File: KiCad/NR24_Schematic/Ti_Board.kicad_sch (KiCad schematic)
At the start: 23 parts, among them J5 J1 Pin J3 Pin, J5 J12 (CAN Interface w/ Transce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, J5 J4 Pin J2 Pin, J5 J5 Pin J7 Pin, J5 J8 Pin J6 Pin, J5 XBEE PRO, J6 SpeakON_NL2, Q1 Q_NMOS_DGS, Q2 Q_NMOS_DGS, Q3 Q_NMOS_DGS

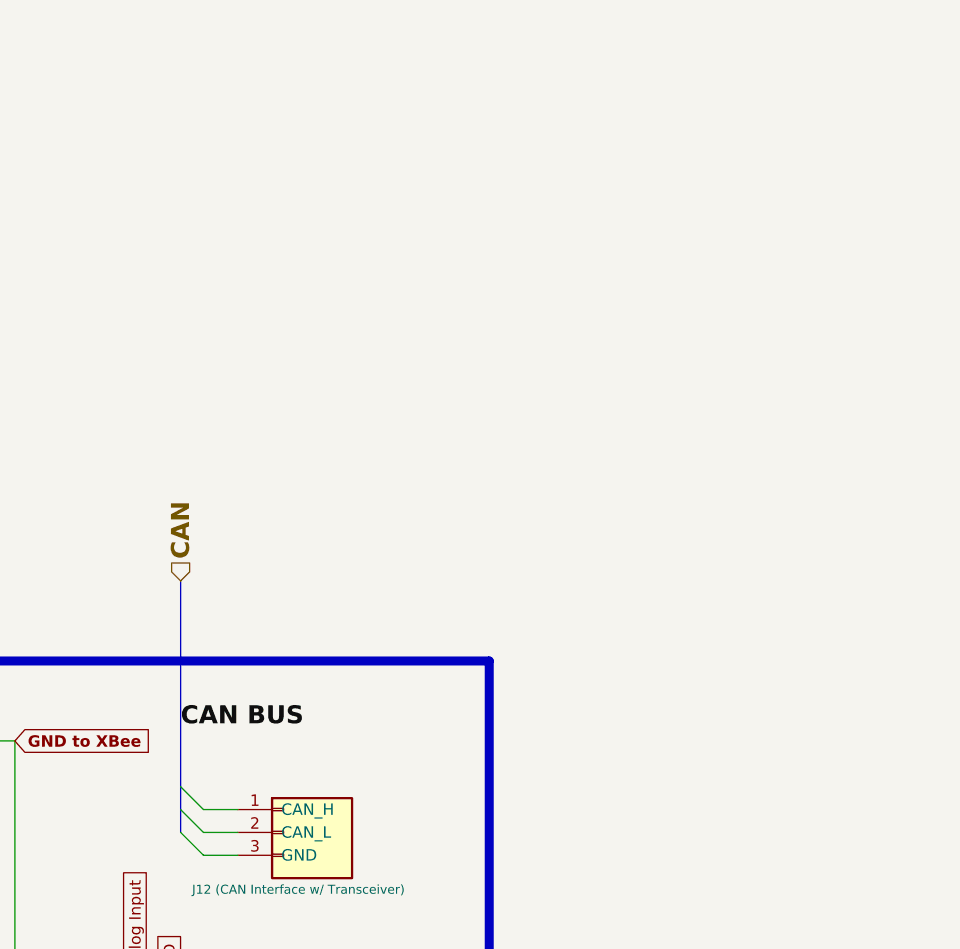
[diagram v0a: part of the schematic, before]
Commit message: Please add locations
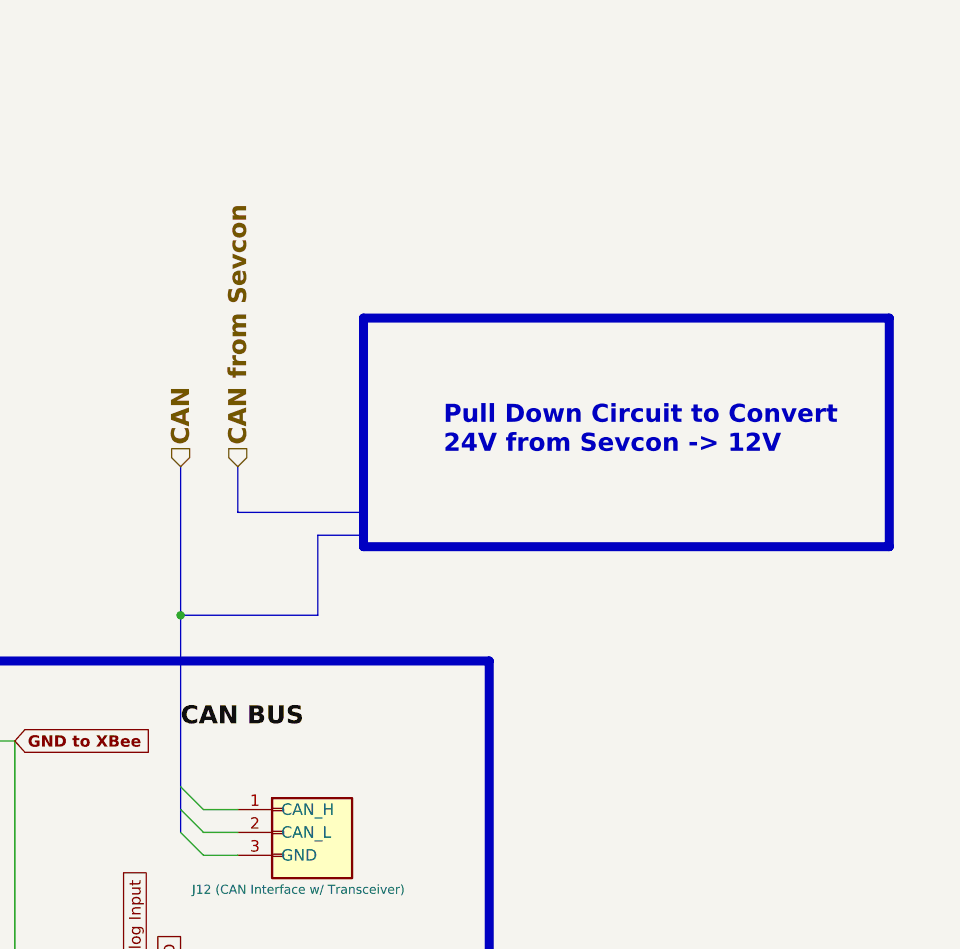
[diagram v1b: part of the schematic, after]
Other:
- note added: "Pull Down Circuit to Convert 24V from Sevcon -> 12V"
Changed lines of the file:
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@@
   (junction (at 182.88 50.8) (diameter 0) (color 0 0 0 0)
+  )
+  (junction (at 288.29 120.65) (diameter 0) (color 0 0 0 0)
   )
   (junction (at 139.7 62.23) (diameter 0) (color 0 0 0 0)
@@
     (stroke (width 0) (type default))
   )
+  (bus (pts (xy 303.53 111.76) (xy 308.61 111.76))
+    (stroke (width 0.75) (type default) (color 0 132 132 1))
+  )
+  (bus (pts (xy 294.64 104.14) (xy 294.64 109.22))
+    (stroke (width 0.75) (type default) (color 0 132 132 1))
+  )
   (wire (pts (xy 73.66 213.36) (xy 74.93 213.36))
     (stroke (width 0) (type default))
@@
     (stroke (width 0) (type default))
   )
+  (bus (pts (xy 288.29 120.65) (xy 303.53 120.65))
+    (stroke (width 0.75) (type default) (color 0 132 132 1))
+  )
   (wire (pts (xy 33.02 142.24) (xy 34.29 142.24))
     (stroke (width 0) (type default))
@@
   (bus (pts (xy 144.78 85.09) (xy 162.56 85.09))
     (stroke (width 0) (type default))
+  )
+  (bus (pts (xy 294.64 109.22) (xy 308.61 109.22))
+    (stroke (width 0.75) (type default) (color 0 132 132 1))
   )
   (wire (pts (xy 182.88 50.8) (xy 182.88 45.72))
@@
     (stroke (width 0) (type default))
   )
+  (bus (pts (xy 288.29 120.65) (xy 288.29 139.7))
+    (stroke (width 0.75) (type default) (color 0 132 132 1))
+  )
   (wire (pts (xy 232.41 152.4) (xy 232.41 99.06))
     (stroke (width 0) (type default))
@@
     (stroke (width 0) (type default))
   )
-  (bus (pts (xy 288.29 116.84) (xy 288.29 139.7))
+  (bus (pts (xy 288.29 104.14) (xy 288.29 120.65))
     (stroke (width 0.75) (type default) (color 0 132 132 1))
   )
@@
   (wire (pts (xy 25.4 210.82) (xy 31.75 210.82))
     (stroke (width 0) (type default))
+  )
+  (bus (pts (xy 303.53 120.65) (xy 303.53 111.76))
+    (stroke (width 0.75) (type default) (color 0 132 132 1))
   )
   (wire (pts (xy 104.14 88.9) (xy 121.92 88.9))
@@
   (rectangle (start 17.78 201.93) (end 175.26 247.65)
     (stroke (width 1) (type default) (color 132 0 0 1))
+    (fill (type none))
+  )
+  (rectangle (start 308.61 87.63) (end 367.03 113.03)
+    (stroke (width 1) (type default))
     (fill (type none))
   )
@@
     (effects (font (size 3 3) (thickness 0.4) bold) (justify left bottom))
   )
+  (text "Pull Down Circuit to Convert\n24V from Sevcon -> 12V\n"
+    (at 317.5 102.87 0)
+    (effects (font (size 2 2) bold) (justify left bottom))
+  )
   (text "XBee" (at 322.58 248.92 0)
     (effects (font (size 3 3)) (justify left bottom))
@@
     )
   )
-  (hierarchical_label "CAN" (shape input) (at 288.29 116.84 90) (fields_autoplaced)
+  (hierarchical_label "CAN" (shape input) (at 288.29 104.14 90) (fields_autoplaced)
     (effects (font (size 2 2) (thickness 0.4) bold (color 0 194 194 1)) (justify left))
   )
@@
     (effects (font (size 1.27 1.27)) (justify right))
   )
+  (hierarchical_label "CAN from Sevcon" (shape input) (at 294.64 104.14 90) (fields_autoplaced)
+    (effects (font (size 2 2) bold (color 0 194 194 1)) (justify left))
+  )
   (hierarchical_label "To Dash" (shape input) (at 200.66 99.06 180) (fields_autoplaced)

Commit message: .
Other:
- note added: "Lights Logic on the Dash AND Break Light (to be continued)"
- note removed: "Lights Logic on the Dash (to be continued)"
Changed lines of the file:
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@@
   (junction (at 288.29 120.65) (diameter 0) (color 0 0 0 0)
   )
+  (junction (at 107.95 85.09) (diameter 0) (color 0 0 0 0)
+  )
   (junction (at 139.7 62.23) (diameter 0) (color 0 0 0 0)
   )
@@
   )
   (bus (pts (xy 119.38 85.09) (xy 137.16 85.09))
+    (stroke (width 0) (type default))
+  )
+  (bus (pts (xy 107.95 85.09) (xy 110.49 85.09))
     (stroke (width 0) (type default))
   )
@@
     (stroke (width 0) (type default))
   )
-  (bus (pts (xy 106.68 85.09) (xy 110.49 85.09))
+  (bus (pts (xy 106.68 85.09) (xy 107.95 85.09))
     (stroke (width 0) (type default))
   )
@@
     (stroke (width 0) (type default))
   )
+  (bus (pts (xy 107.95 81.28) (xy 107.95 85.09))
+    (stroke (width 0) (type default))
+  )
   (wire (pts (xy 95.25 139.7) (xy 96.52 139.7))
     (stroke (width 0) (type default))
@@
   )
   (wire (pts (xy 25.4 210.82) (xy 31.75 210.82))
+    (stroke (width 0) (type default))
+  )
+  (bus (pts (xy 106.68 81.28) (xy 107.95 81.28))
     (stroke (width 0) (type default))
   )
@@
     (effects (font (face "Britannic Bold") (size 1.5 1.5)) (justify left bottom))
   )
-  (text "Lights Logic on the Dash (to be continued)" (at 91.44 24.13 0)
+  (text "Lights Logic on the Dash AND Break Light (to be continued)"
+    (at 91.44 24.13 0)
     (effects (font (size 3 3) (thickness 0.4) bold) (justify left bottom))
   )
@@
     (effects (font (size 2 2) bold (color 0 194 194 1)) (justify left))
   )
+  (hierarchical_label "Break Light" (shape input) (at 106.68 81.28 180) (fields_autoplaced)
+    (effects (font (size 1.27 1.27)) (justify right))
+  )
   (hierarchical_label "To Dash" (shape input) (at 200.66 99.06 180) (fields_autoplaced)

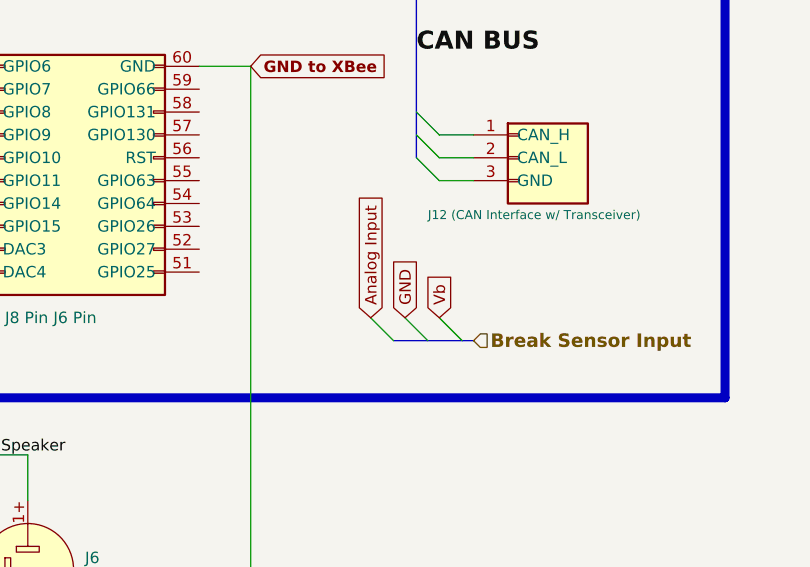
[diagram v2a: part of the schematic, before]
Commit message: added accumulator info
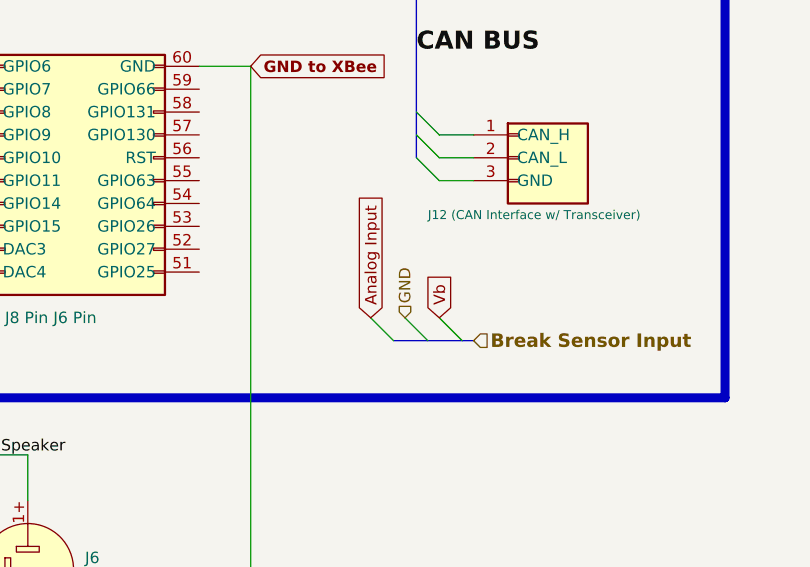
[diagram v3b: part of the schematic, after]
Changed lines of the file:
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@@
-    )
-  )
-  (global_label "GND" (shape input) (at 287.02 162.56 90) (fields_autoplaced)
-    (effects (font (size 1.27 1.27)) (justify left))
-    (property "Intersheetrefs" "${INTERSHEET_REFS}" (at 287.02 155.7043 90)
-      (effects (font (size 1.27 1.27)) (justify right) hide)
     )
   )
@@
     (effects (font (size 1.27 1.27)) (justify right))
   )
+  (hierarchical_label "GND" (shape input) (at 287.02 162.56 90) (fields_autoplaced)
+    (effects (font (size 1.27 1.27)) (justify left))
+  )
   (hierarchical_label "CAN from Sevcon" (shape input) (at 294.64 104.14 90) (fields_autoplaced)
     (effects (font (size 2 2) bold (color 0 194 194 1)) (justify left))
@@
     (pin "3")
     (instances
-      (project "Car_TractiveSystem_v2"
+      (project "Car_TractiveSystem_MAIN"
         (path "/588b5c14-1813-4e1d-9dbe-940839ecebe3/42103732-fa28-467e-b394-54af70cbf903"
           (reference "Q3") (unit 1)
@@
     (pin "2")
     (instances
-      (project "Car_TractiveSystem_v2"
+      (project "Car_TractiveSystem_MAIN"
         (path "/588b5c14-1813-4e1d-9dbe-940839ecebe3/42103732-fa28-467e-b394-54af70cbf903"
           (reference "D3") (unit 1)
@@
     (pin "40")
     (instances
-      (project "Car_TractiveSystem_v2"
+      (project "Car_TractiveSystem_MAIN"
         (path "/588b5c14-1813-4e1d-9dbe-940839ecebe3"
           (reference "J5") (unit 1)
@@
     (pin "3")
     (instances
-      (project "Car_TractiveSystem_v2"
+      (project "Car_TractiveSystem_MAIN"
         (path "/588b5c14-1813-4e1d-9dbe-940839ecebe3/42103732-fa28-467e-b394-54af70cbf903"
           (reference "Q1") (unit 1)
@@
     (pin "80")
     (instances
-      (project "Car_TractiveSystem_v2"
+      (project "Car_TractiveSystem_MAIN"
         (path "/588b5c14-1813-4e1d-9dbe-940839ecebe3"
           (reference "J5") (unit 1)
@@
     (pin "9")
     (instances
-      (project "Car_TractiveSystem_v2"
+      (project "Car_TractiveSystem_MAIN"
         (path "/588b5c14-1813-4e1d-9dbe-940839ecebe3"
           (reference "J5") (unit 1)
@@
     (pin "9")
     (instances
-      (project "Car_TractiveSystem_v2"
+      (project "Car_TractiveSystem_MAIN"
         (path "/588b5c14-1813-4e1d-9dbe-940839ecebe3"
           (reference "J5") (unit 1)
@@
     (pin "70")
     (instances
-      (project "Car_TractiveSystem_v2"
+      (project "Car_TractiveSystem_MAIN"
         (path "/588b5c14-1813-4e1d-9dbe-940839ecebe3"
           (reference "J5") (unit 1)
@@
     (pin "1+")
     (instances
-      (project "Car_TractiveSystem_v2"
+      (project "Car_TractiveSystem_MAIN"
         (path "/588b5c14-1813-4e1d-9dbe-940839ecebe3/42103732-fa28-467e-b394-54af70cbf903"
           (reference "J6") (unit 1)
@@
     (pin "40")
     (instances
-      (project "Car_TractiveSystem_v2"
+      (project "Car_TractiveSystem_MAIN"
         (path "/588b5c14-1813-4e1d-9dbe-940839ecebe3"
           (reference "J5") (unit 1)
@@
     (pin "3")
     (instances
-      (project "Car_TractiveSystem_v2"
+      (project "Car_TractiveSystem_MAIN"
         (path "/588b5c14-1813-4e1d-9dbe-940839ecebe3/42103732-fa28-467e-b394-54af70cbf903"
           (reference "Q2") (unit 1)
@@
     (pin "2")
     (instances
-      (project "Car_TractiveSystem_v2"
+      (project "Car_TractiveSystem_MAIN"
         (path "/588b5c14-1813-4e1d-9dbe-940839ecebe3/42103732-fa28-467e-b394-54af70cbf903"
           (reference "R2") (unit 1)
@@
     (pin "2")
     (instances
-      (project "Car_TractiveSystem_v2"
+      (project "Car_TractiveSystem_MAIN"
         (path "/588b5c14-1813-4e1d-9dbe-940839ecebe3/42103732-fa28-467e-b394-54af70cbf903"
           (reference "R4") (unit 1)
@@
     (pin "3")
     (instances
-      (project "Car_TractiveSystem_v2"
+      (project "Car_TractiveSystem_MAIN"
         (path "/588b5c14-1813-4e1d-9dbe-940839ecebe3"
           (reference "J5") (unit 1)
@@
     (pin "2")
     (instances
-      (project "Car_TractiveSystem_v2"
+      (project "Car_TractiveSystem_MAIN"
         (path "/588b5c14-1813-4e1d-9dbe-940839ecebe3/42103732-fa28-467e-b394-54af70cbf903"
           (reference "R4") (unit 1)
@@
     (pin "2")
     (instances
-      (project "Car_TractiveSystem_v2"
+      (project "Car_TractiveSystem_MAIN"
         (path "/588b5c14-1813-4e1d-9dbe-940839ecebe3/42103732-fa28-467e-b394-54af70cbf903"
           (reference "R2") (unit 1)
@@
     (pin "2")
     (instances
-      (project "Car_TractiveSystem_v2"
+      (project "Car_TractiveSystem_MAIN"
         (path "/588b5c14-1813-4e1d-9dbe-940839ecebe3/42103732-fa28-467e-b394-54af70cbf903"
           (reference "R4") (unit 1)
@@
     (pin "9")
     (instances
-      (project "Car_TractiveSystem_v2"
+      (project "Car_TractiveSystem_MAIN"
         (path "/588b5c14-1813-4e1d-9dbe-940839ecebe3"
           (reference "J5") (unit 1)
@@
     (pin "2")
     (instances
-      (project "Car_TractiveSystem_v2"
+      (project "Car_TractiveSystem_MAIN"
         (path "/588b5c14-1813-4e1d-9dbe-940839ecebe3/42103732-fa28-467e-b394-54af70cbf903"
           (reference "D3") (unit 1)
@@
     (pin "2")
     (instances
-      (project "Car_TractiveSystem_v2"
+      (project "Car_TractiveSystem_MAIN"
         (path "/588b5c14-1813-4e1d-9dbe-940839ecebe3/42103732-fa28-467e-b394-54af70cbf903"
           (reference "R2") (unit 1)
@@
     (pin "2")
     (instances
-      (project "Car_TractiveSystem_v2"
+      (project "Car_TractiveSystem_MAIN"
         (path "/588b5c14-1813-4e1d-9dbe-940839ecebe3/42103732-fa28-467e-b394-54af70cbf903"
           (reference "R3") (unit 1)
@@
     (pin "2")
     (instances
-      (project "Car_TractiveSystem_v2"
+      (project "Car_TractiveSystem_MAIN"
         (path "/588b5c14-1813-4e1d-9dbe-940839ecebe3/42103732-fa28-467e-b394-54af70cbf903"
           (reference "R4") (unit 1)
@@
     (pin "2")
     (instances
-      (project "Car_TractiveSystem_v2"
+      (project "Car_TractiveSystem_MAIN"
         (path "/588b5c14-1813-4e1d-9dbe-940839ecebe3/42103732-fa28-467e-b394-54af70cbf903"
           (reference "D3") (unit 1)

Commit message: Pre Break Schematic
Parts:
- renumbered D3 to D1, D3 to D2, J6 to J11, R4 to R1, R4 to R2, R4 to R3, R3 to R4, R4 to R5, R2 to R6, R2 to R7, R2 to R8
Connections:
- net GND: no longer J11.1-, J5.62 (GND)
- net BLK: no longer names the net of D2.2 (A), Q1.3 (S), Q2.3 (S), Q3.2 (G), R1.1, R2.1, R4.1
- net BLK: no longer D1.2 (A), D3.2 (A), Q1.1 (D), Q2.1 (D)
- net Ready to Drive Speaker: no longer names the net of J11.1+, J5.63 (ADCIN15)
- new net: D3.2 (A), Q1.1 (D)
- new net: J11.1-, J5.62 (GND)
- new net: D1.2 (A), Q2.1 (D)
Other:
- note added: "BLCK GND"
- note added: "BLK"
- note added: "CAN Bus"
- note added: "FWD BTTN (Black, Green) NTL BTTN (GRN BLCK) ROCKER SWITCH (Black, Yellow) EMCY BTTN (Black, Green)"
- note added: "GND"
- note added: "GRN"
- note added: "Ready to Drive Speaker"
- note added: "brown wire"
